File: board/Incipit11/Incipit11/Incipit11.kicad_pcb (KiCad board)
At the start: 2 copper layers, 39.4 x 39.4 mm, 34 parts, among them J1 SM04B-SRSS-TB_LF__SN_, J2 Conn_01x03, J3 Conn_02x03_Odd_Even, J4 Conn_01x02, J5 284391-6, Q1 MCU30N02-TP, U1 ATTINY3224-XUR, U2 EL0631(TA), U3 SPX1117M3-L-3-3/TR

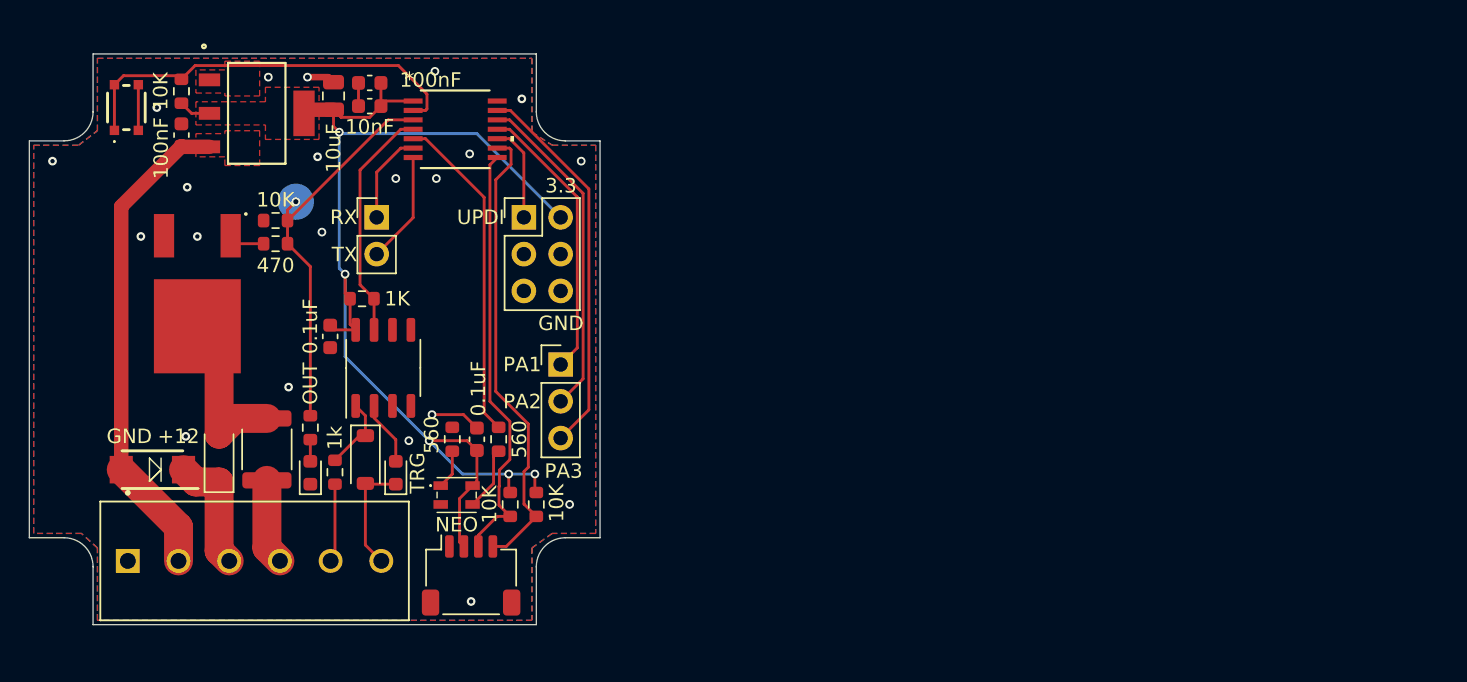
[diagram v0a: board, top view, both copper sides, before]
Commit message: Rev B of board for new case. Did a few modifications to add more reverse protection on output and changed the I2C to seperate the 3.3 power from controller and peripheral.
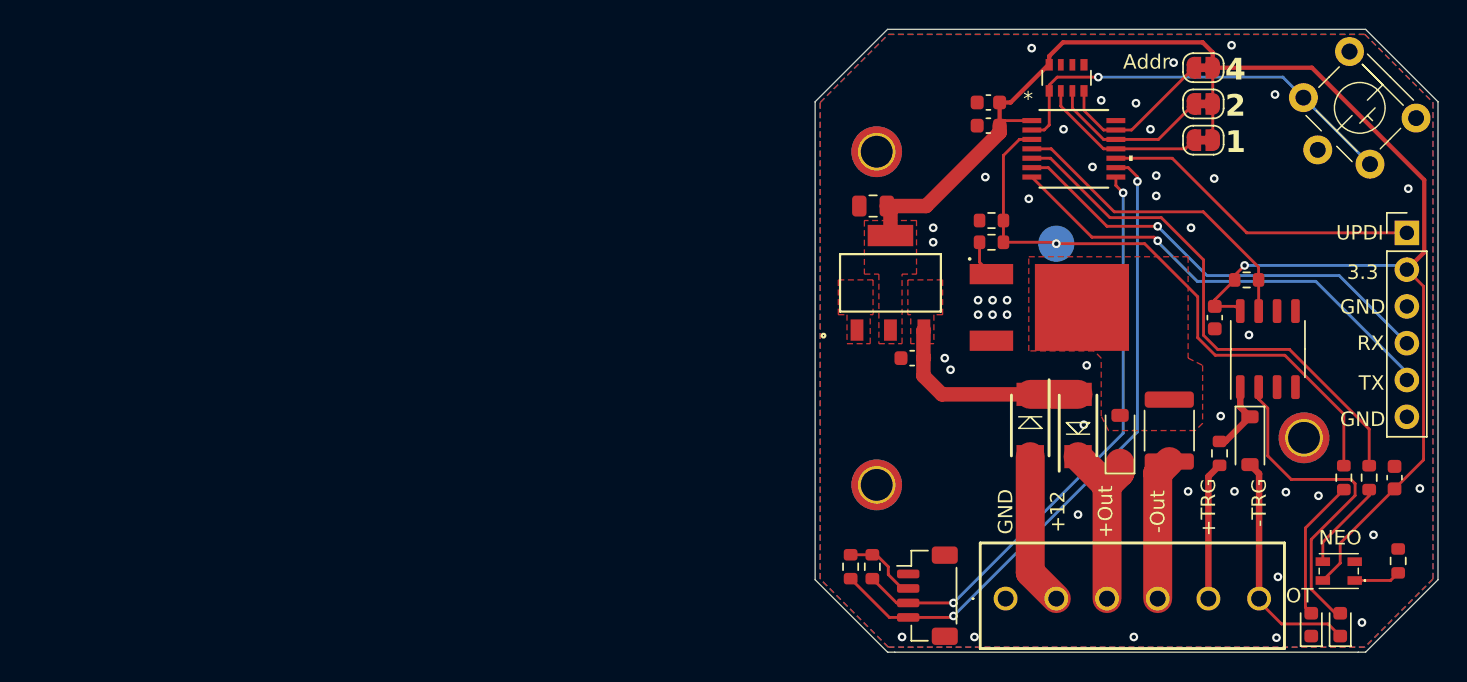
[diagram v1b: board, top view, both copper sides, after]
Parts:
- removed J4: Conn_01x02, Connector_PinHeader_2.54mm:PinHeader_1x02_P2.54mm_Vertical
- removed J5: 284391-6, Department of Alchemy:TE_284391-6
- removed R10: 10K, Resistor_SMD:R_0603_1608Metric
- removed S1: TL1018AAAF160QG, Department of Alchemy:TL1018AAAF160QG
- added D6: SL54AFL-TP, Department of Alchemy:SL54AFL-TP DO-221AC(SMA-FL), F.Cu at (139.1, 95.5)
- added H1: MountingHole_Pad, MountingHole:MountingHole_2.2mm_M2_ISO7380_Pad_TopBottom, F.Cu at (128.5, 99.8)
- added H2: MountingHole_Pad, MountingHole:MountingHole_2.2mm_M2_ISO7380_Pad_TopBottom, F.Cu at (128.5, 76.8)
- added H3: MountingHole_Pad, MountingHole:MountingHole_2.2mm_M2_ISO7380_Pad_TopBottom, F.Cu at (158.0, 96.5)
- added JP1: ADDR0, Jumper:SolderJumper-2_P1.3mm_Bridged_RoundedPad1.0x1.5mm, F.Cu at (151.1, 76.0)
- added JP2: ADDR1, Jumper:SolderJumper-2_P1.3mm_Bridged_RoundedPad1.0x1.5mm, F.Cu at (151.1, 73.5)
- added JP3: ADDR2, Jumper:SolderJumper-2_P1.3mm_Bridged_RoundedPad1.0x1.5mm, F.Cu at (151.1, 71.0)
- added RN1: 10K, Resistor_SMD:R_Array_Convex_4x0603, F.Cu at (141.6, 71.7)
- added SW2: SW_Push_Shielded, Department of Alchemy:CT1102P, F.Cu at (161.8, 73.7)
- C1, C6: value 100nF -> 0.1uF
- J1: footprint Department of Alchemy:JST_SH_SM04B-SRSS-TB_1x04-1MP_P1.00mm_Horizontal -> Department of Alchemy:JST_SH_BM04B-SRSS-TB_1x04-1MP_P1.00mm_Vertical
- J2: value Conn_01x03 -> 2383942-6; footprint Connector_PinHeader_2.54mm:PinHeader_1x03_P2.54mm_Vertical -> Department of Alchemy:393570006
- J3: value Conn_02x03_Odd_Even -> Conn_01x06; footprint Connector_PinHeader_2.54mm:PinHeader_2x03_P2.54mm_Vertical -> Connector_PinHeader_2.54mm:PinHeader_1x06_P2.54mm_Vertical
- R3: value 1k -> 1K
- moved R7 71.4 mm to (160.8, 99.2)
- moved D4 69.9 mm to (158.5, 109.4)
- moved D2 66.0 mm to (160.5, 109.4)
- moved R6 65.8 mm to (164.5, 105.0)
- moved D3 63.8 mm to (142.4, 95.8), turned to 90 degrees
- moved C3 63.4 mm to (164.2, 99.2)
- moved F1 62.3 mm to (148.7, 96.0)
- moved D5 62.2 mm to (145.3, 96.6)
- moved LED1 61.1 mm to (160.4, 105.7), turned to 0 degrees
- moved C4 61.1 mm to (151.8, 88.2)
- moved D1 61.1 mm to (154.3, 96.7)
- moved R5 61.1 mm to (154.0, 85.6)
- moved Q1 61.1 mm to (142.7, 87.5), turned to -90 degrees
- moved R3 61.1 mm to (152.2, 97.6)
- moved U2 61.1 mm to (155.5, 90.4)
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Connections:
- J1 pad 2: +3.3V -> +3.3VP
- J2 pad 1: /PA1 -> GND
- J2 pad 2: /PA2 -> Net-(D6-A)
- J2 pad 3: /PA3 -> +12P
- J3 pad 3: unconnected-(J3-Pin_3-Pad3) -> GND
- J3 pad 4: unconnected-(J3-Pin_4-Pad4) -> /RX
- J3 pad 5: unconnected-(J3-Pin_5-Pad5) -> /TX
- R1 pad 1: +3.3V -> +3.3VP
- R2 pad 1: +3.3V -> +3.3VP
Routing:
- net /RX: track 6.32 -> 30.9 mm, vias 0 -> 1
- net /TX: track 7.71 -> 32.0 mm, vias 0 -> 1
- net +3.3V: track 83.2 -> 106.6 mm, vias 5 -> 1
- net +12V: track 33.9 -> 14.4 mm
- net Net-(D2-A): track 4.45 -> 23.1 mm
- net /UPDI: track 6.69 -> 23.1 mm
- net /PA3: track 26.6 -> 11.3 mm
- net /OutputPWM: track 27.2 -> 42.0 mm
- net /NEOPIXEL: track 22.9 -> 36.6 mm
- net /SCL: track 32.0 -> 45.6 mm, vias 0 -> 2
- net Net-(D5-A): track 11.8 -> 0.00 mm
- net /PA2: track 23.0 -> 11.5 mm
- net /SDA: track 29.7 -> 40.8 mm, vias 0 -> 2
- net Net-(D6-A): track 0.00 -> 10.5 mm
- net GND: track 10.2 -> 0.00 mm, vias 21 -> 43
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- added copper zone on F.Cu, net Net-(D5-A)
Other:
- board size 39.4 x 39.4 mm -> 43 x 43 mm
- board text added: "+Out"
- board text added: "+TRG"
- board text added: "-Out"
- board text added: "-TRG"
- board text added: "1"
- board text added: "2"
- board text added: "4"
- board text added: "Addr"
- board text added: "B"
- board text added: "OT"
- board text removed: "A"
- board text removed: "OUT"
- board text removed: "PA1"
- board text removed: "PA2"
- board text removed: "PA3"
- board text removed: "TRG"
